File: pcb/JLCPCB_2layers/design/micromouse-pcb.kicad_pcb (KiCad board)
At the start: 2 copper layers, 100 x 120 mm, 139 parts, among them J1 JST_XH_B2B-XH-A_1x02_P2.50mm_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, J10 AMASS_XT60-M_1x02_P7.20mm_Ver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, J5 JST_ZH_B6B-ZR_1x06_P1.50mm_Ve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, J6 JST_ZH_B6B-ZR_1x06_P1.50mm_Ve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, J7 USB_C_Receptacle_GCT_USB4105-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, J9 JST_XH_B3B-XH-A_1x03_P2.50mm_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, Q1 SOT-23, Q16 SOT-23, Q17 SOT-23, Q18 SOT-23, Q2 LED_D5.0mm_IRBlack, Q28 SOT-23, Q29 SOT-23, Q3 LED_D5.0mm_IRBlack, Q30 SOT-23, Q31 SOT-23, Q32 SOT-23, Q33 SOT-23, Q34 SOT-23, Q4 LED_D5.0mm_IRBlack, Q5 LED_D5.0mm_IRBlack, Q6 LED_D5.0mm_IRBlack, Q7 LED_D5.0mm_IRBlack, SW1 SW_PUSH_6mm, SW2 SW_PUSH_6mm, SW3 SW_PUSH_6mm, SW4 SW_PUSH_6mm, SW5 SW_SPDT_PCM12, SW6 SW_SPDT_PCM12, U1 TSOT-23-6, U2 SSOP-24_5.3x8.2mm_P0.65mm, U3 ESP32-S3-WROOM-1, U6 SOT-23-6, U7 SOT-23-6, U8 VAL

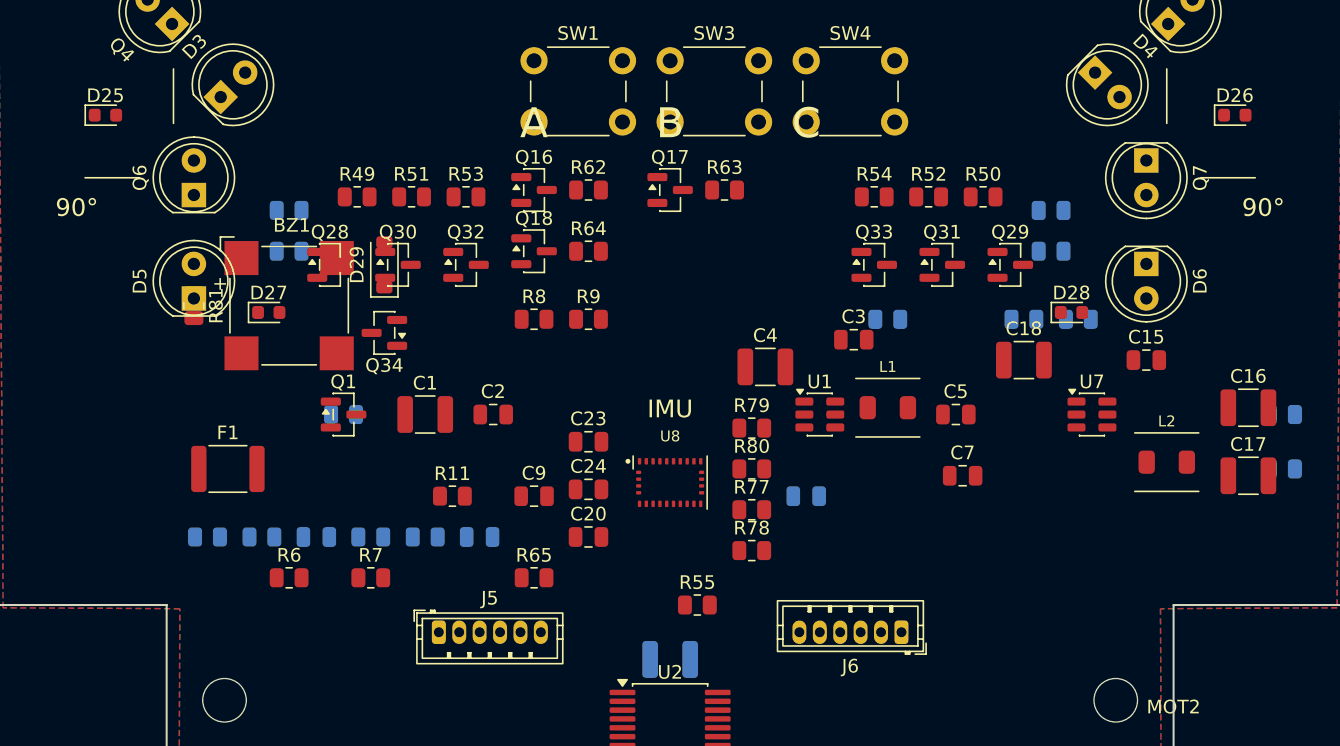
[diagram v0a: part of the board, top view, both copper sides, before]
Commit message: 2-layer: J5/J6 true symmetry + D25/D26 inboard (user render feedback)
- J5 nudged forward 0.9mm so its connector BODY-centre y (69.55) matches J6's
  -- the rot-180 mirror had shifted J6's body 0.9mm forward, leaving J5 looking
  behind. Now mirror-symmetric in both axes (X 36.8<->63.3, Y both 69.55).
  Relocated the R6/R7/R65 resistor row that blocked J5's forward path into the
  front-mid freed space.
- Wall indicators D25/D26 moved INBOARD (x8.5/91.5 -> 30/70), behind the
  diagonal/side sensors and out of the IR beam path (user).

No courtyard overlaps; ERC 0; 138 components.

Co-Authored-By: Claude Fable 5 <noreply@anthropic.com>
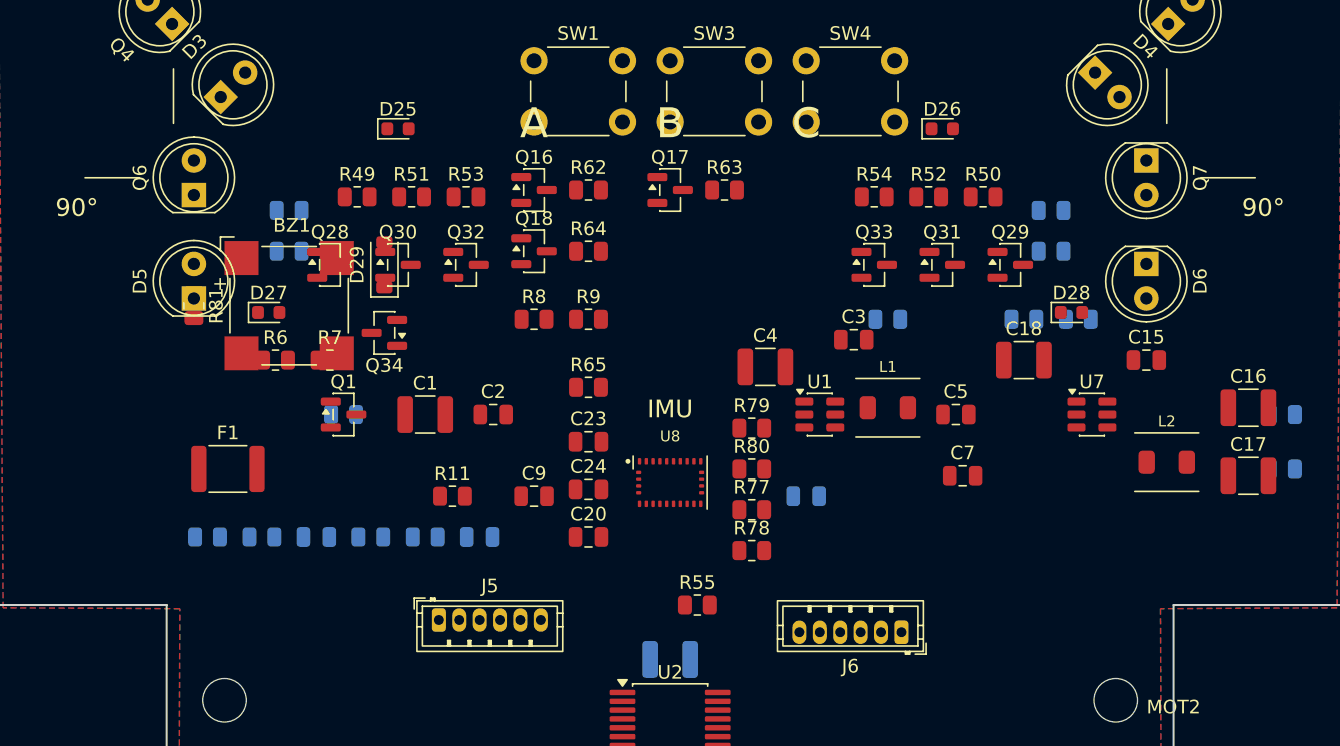
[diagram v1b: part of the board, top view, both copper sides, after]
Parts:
- moved D25 21.5 mm to (30.0, 33.0)
- moved D26 21.5 mm to (70.0, 33.0)
- moved R7 16.3 mm to (25.0, 50.0)
- moved R6 16.0 mm to (21.0, 50.0)
- moved R65 14.6 mm to (44.0, 52.0)
- moved J5 0.90 mm to (33.0, 69.1)

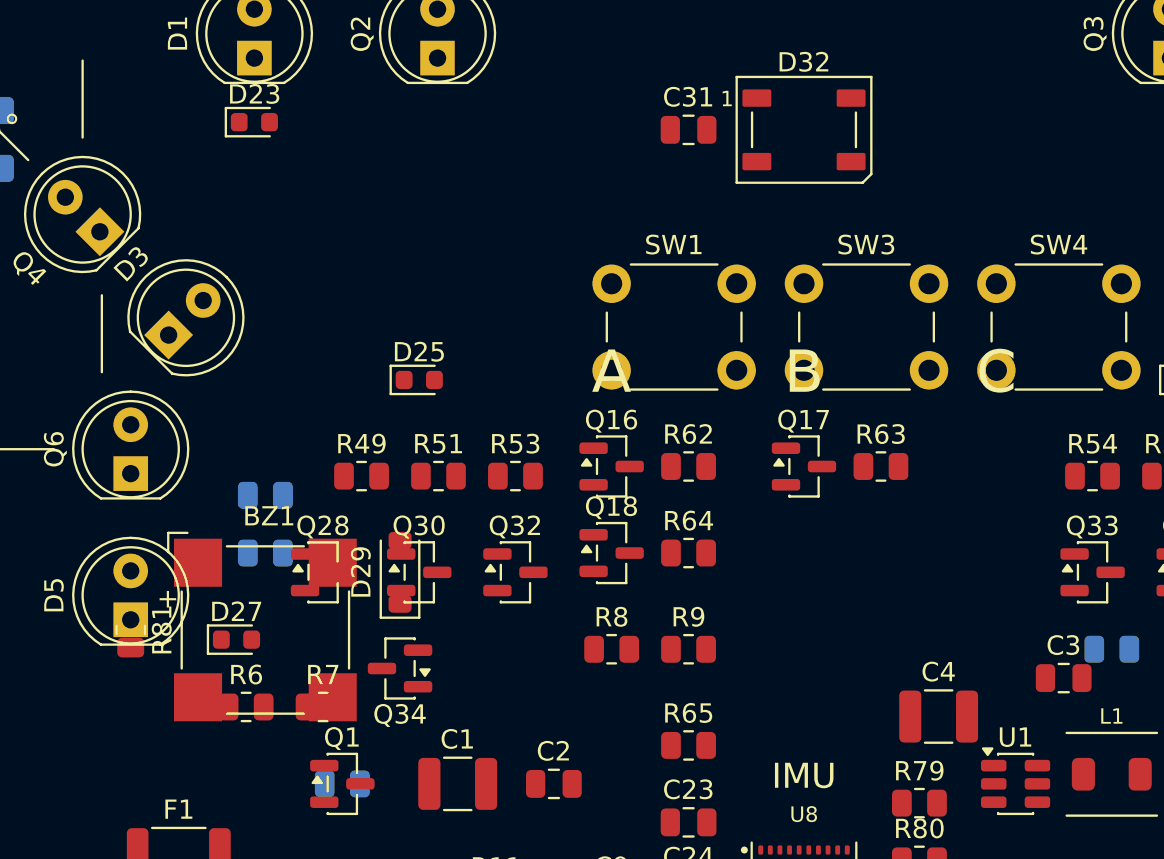
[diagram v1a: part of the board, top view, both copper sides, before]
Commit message: 2-layer: fix the overlap-check hole + move buzzer to the clear bottom
- Overlap-check gap fixed (user: "why no checks for overlap, buzzer overlapped"):
  the CUI buzzer footprint ships a DEGENERATE courtyard (1 point), so the check
  silently skipped it -- BZ1 was buried under 9 parts and never flagged. The
  check now falls back to the footprint body bbox for any near-zero-area
  courtyard, so this class of part is guarded going forward.
- Buzzer relocated: the TOP face has ZERO clear 9mm spots (dense); the removed
  line array left the whole BOTTOM-front open, so the 8.5mm BZ1 + its driver
  (Q34/D29/R81) moved to the bottom-front with generous margin.
- With the fixed check, a hidden C4<->U1 0.3mm tightness surfaced -> C4 nudged
  clear of the buck corner.

No courtyard overlaps; ERC 0. Both top+bottom renders refreshed.

Co-Authored-By: Claude Fable 5 <noreply@anthropic.com>
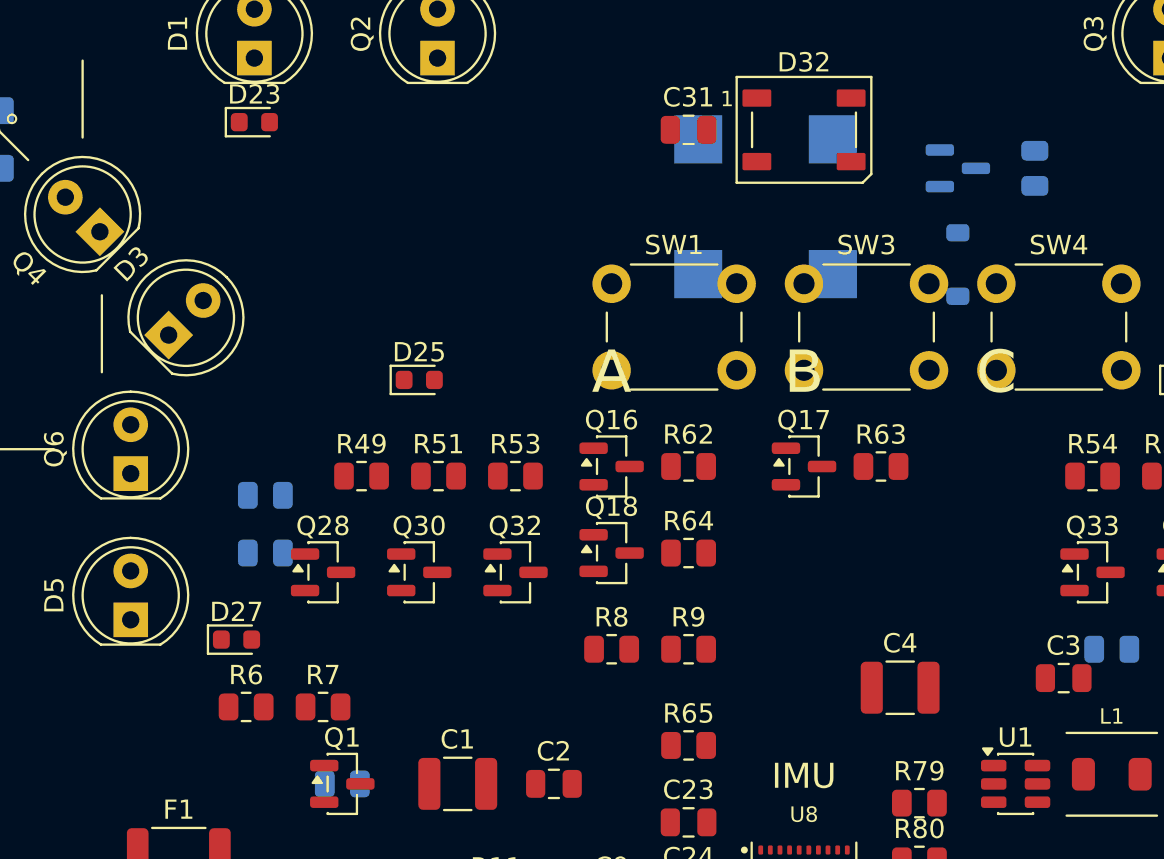
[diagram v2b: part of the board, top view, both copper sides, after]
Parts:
- BZ1, D29, Q34, R81: moved to B.Cu
- moved R81 52.8 mm to (62.0, 22.0)
- moved Q34 38.9 mm to (58.0, 22.0), turned to 0 degrees
- moved BZ1 34.1 mm to (48.0, 24.0), turned to 180 degrees
- moved D29 33.1 mm to (58.0, 27.0)
- moved C4 2.50 mm to (55.0, 49.0)

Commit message: 2-layer: buzzer back on TOP (the top was NOT full -- silk inflated the scan)
User was right: the "top is full" conclusion came from a scan that counted
silk labels as occupied space. A PAD-based scan finds real top spots forward
of the RGB and beside the motor connectors. Buzzer BZ1 moved to the TOP face
beside J6 (open right-mid area); its driver (Q34/D29/R81) rides on the bottom
beneath it. No courtyard overlaps; ERC 0. Both renders refreshed.

Co-Authored-By: Claude Fable 5 <noreply@anthropic.com>
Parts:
- BZ1: moved to F.Cu
- moved BZ1 48.4 mm to (78.0, 62.0), turned to 0 degrees
- moved Q34 46.2 mm to (72.0, 66.0)
- moved D29 45.2 mm to (84.0, 64.0)
- moved R81 42.2 mm to (66.0, 64.0)

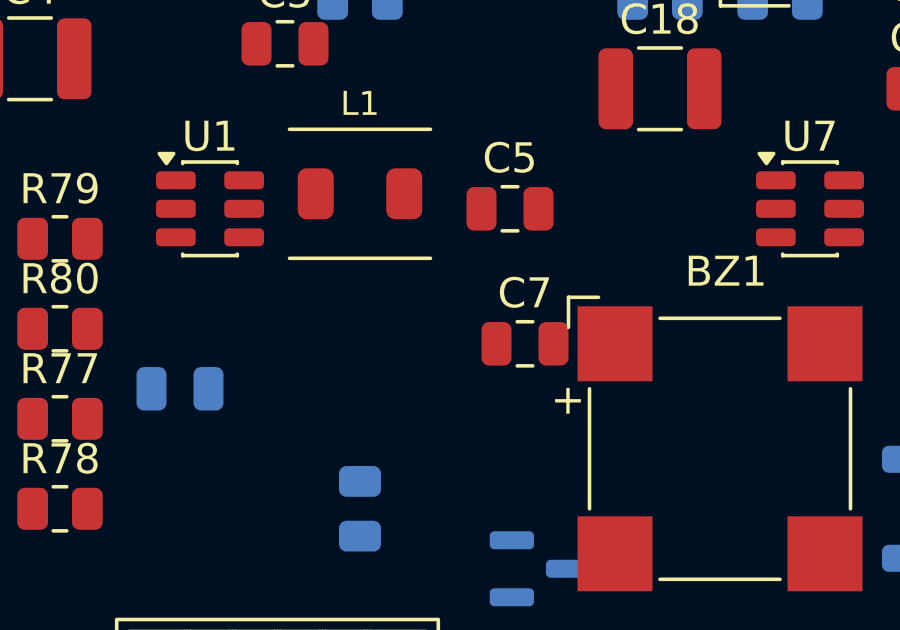
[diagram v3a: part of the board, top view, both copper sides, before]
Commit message: 2-layer: move C7 5mm left, clear of the buzzer (user)
C7 (22uF) 71.5 -> 66.5mm; body gap to BZ1 now 5.65mm (was 0.65). No overlaps.

Co-Authored-By: Claude Fable 5 <noreply@anthropic.com>
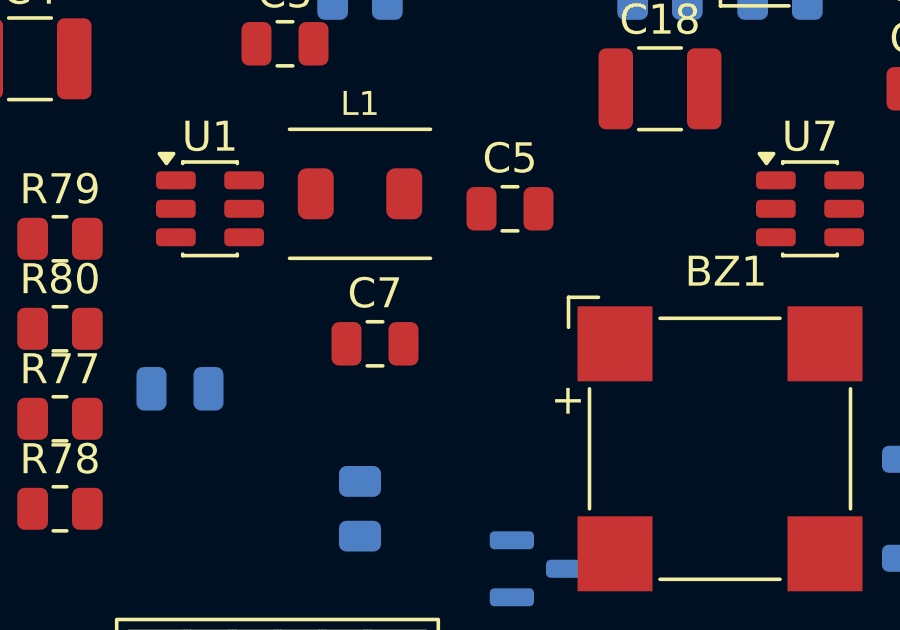
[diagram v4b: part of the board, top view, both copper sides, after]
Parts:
- moved C7 5.00 mm to (66.5, 58.5)

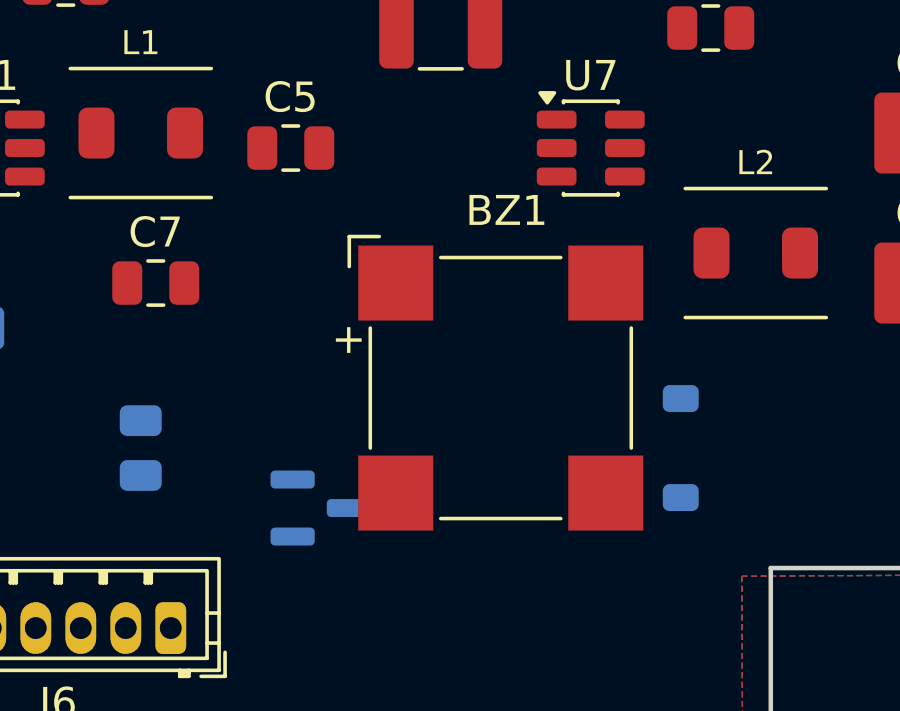
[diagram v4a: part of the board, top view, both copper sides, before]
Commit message: 2-layer: move BZ1 (buzzer) 2mm left (user)
BZ1 78 -> 76mm. No courtyard overlaps; all placement gates clean.

Co-Authored-By: Claude Fable 5 <noreply@anthropic.com>
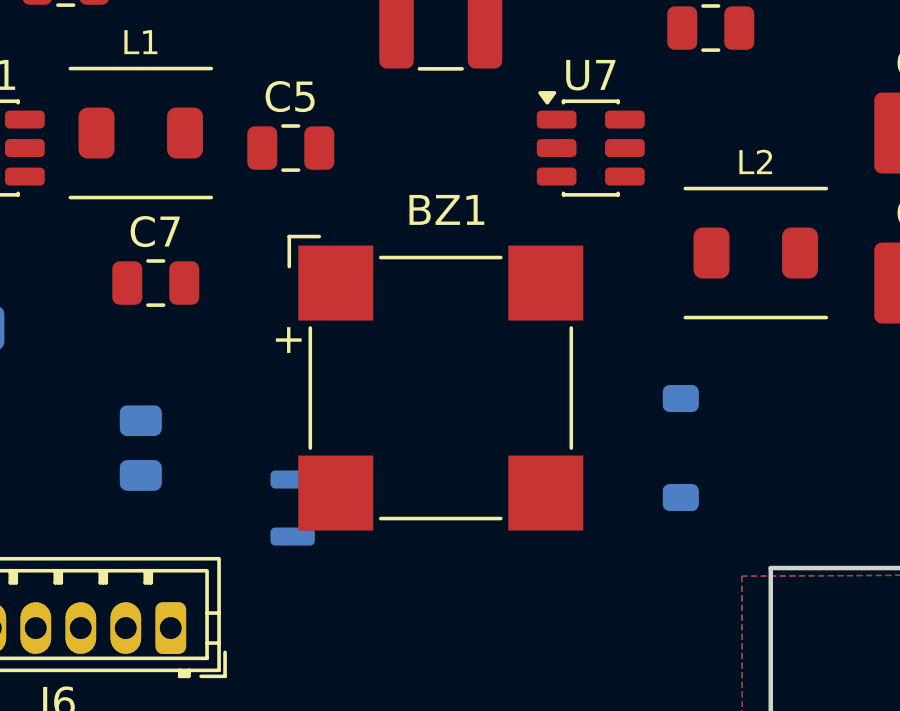
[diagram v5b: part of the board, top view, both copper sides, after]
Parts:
- moved BZ1 2.00 mm to (76.0, 62.0)
